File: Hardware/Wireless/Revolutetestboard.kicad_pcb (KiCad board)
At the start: 4 copper layers, 54 x 85.6 mm, 104 parts, among them J1 -, J2 +, J3 USB_C_Receptacle_USB2.0, J4 Conn_01x02_Pin, J5 USB_C_Receptacle_USB2.0, Q1 NMOS, Q2 NMOS-CSD17381F4, Q3 NMOS-CSD17381F4, Q4 PMOS-CSD25483F4, Q5 PMOS-CSD25483F4, SW1 SW_DIP_x05, U10 Button, U11 LSM6DSO, U12 STM32F103C8Tx, U13 AP2112K-3.3, U14 Conn_01x14_Socket, U2 nrf52833_qfn40, U3 AS5600, U4 MIC5504, U5 BQ24075RGT, U6 Button, U7 Conn_01x14_Socket, U8 Button, U9 Button, X1 32.768 kHz, X2 32MHZ, Y1 32.768KHZ, Y2 8Mhz

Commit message: new flex and new pcbs
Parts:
- removed ? (x2): , 
- added J6: Conn_01x04_Socket, Connector_PinSocket_2.54mm:PinSocket_1x04_P2.54mm_Vertical, F.Cu at (134.8, 140.0)
- added JP6: Jumper_3_Bridged12, Jumper:SolderJumper-3_P1.3mm_Bridged12_RoundedPad1.0x1.5mm, F.Cu at (146.7, 140.0)
- added R23: 2M, Library:Resistor_0402_1005M-nosilk, F.Cu at (153.9, 122.3)
- added SW2: SW_Push, Library:16mmCompButton, B.Cu at (148.5, 99.0)
- added TP1: TestPoint, TestPoint:TestPoint_Pad_D1.0mm, F.Cu at (151.7, 128.7)
- added TP10: TestPoint, TestPoint:TestPoint_Pad_D1.0mm, F.Cu at (146.0, 121.6)
- added TP11: TestPoint, TestPoint:TestPoint_Pad_D1.0mm, F.Cu at (155.2, 121.0)
- added TP12: TestPoint, TestPoint:TestPoint_Pad_D1.0mm, F.Cu at (149.5, 129.6)
- added TP13: TestPoint, TestPoint:TestPoint_Pad_D1.0mm, F.Cu at (141.9, 135.3)
- added TP2: TestPoint, TestPoint:TestPoint_Pad_D1.0mm, F.Cu at (147.9, 135.5)
- added TP3: TestPoint, TestPoint:TestPoint_Pad_D1.0mm, F.Cu at (133.6, 135.3)
- added TP4: TestPoint, TestPoint:TestPoint_Pad_D1.0mm, F.Cu at (114.7, 150.1)
- added TP5: TestPoint, TestPoint:TestPoint_Pad_D1.0mm, F.Cu at (128.1, 127.1)
- added TP6: TestPoint, TestPoint:TestPoint_Pad_D1.0mm, F.Cu at (130.9, 133.3)
- added TP7: TestPoint, TestPoint:TestPoint_Pad_D1.0mm, F.Cu at (130.4, 127.3)
- added TP8: TestPoint, TestPoint:TestPoint_Pad_D1.0mm, F.Cu at (151.4, 133.2)
- added TP9: TestPoint, TestPoint:TestPoint_Pad_D1.0mm, F.Cu at (143.1, 101.1)
- Q1: value NMOS -> PMOS-CSD25483F4
- moved C28 25.1 mm to (122.3, 145.8), turned to -90 degrees
- moved C29 23.9 mm to (121.3, 145.8), turned to -90 degrees
- moved U13 20.7 mm to (118.6, 146.3), turned to 180 degrees
- moved C32 15.8 mm to (117.5, 143.9)
- moved C33 15.3 mm to (119.4, 143.9), turned to 180 degrees
- moved JP4 8.67 mm to (136.8, 124.3), turned to 0 degrees
- moved J4 1.81 mm to (118.2, 141.0)
- moved C25 1.65 mm to (143.1, 131.6)
- moved TH1 1.62 mm to (143.5, 130.1)
- moved R7 1.44 mm to (144.9, 135.4)
- moved D2 1.41 mm to (149.9, 133.6), turned to 90 degrees
- moved R3 1.37 mm to (143.6, 133.8)
- moved R4 1.37 mm to (149.3, 131.1)
- moved R9 1.37 mm to (148.9, 133.6)
- moved U5 1.37 mm to (146.2, 132.3)
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- renumbered AE** to Antenna
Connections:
- Q1 pad 2: MOS_VDD -> VDD_nRF
- Q1 pad 3: VDD_nRF -> MOS_VDD
- SW1 pad 1: unconnected-(SW1-Pad1) -> VBUS
- SW1 pad 2: unconnected-(SW1-Pad2) -> swc
- SW1 pad 3: unconnected-(SW1-Pad3) -> swd
- SW1 pad 4: unconnected-(SW1-Pad4) -> D+
- SW1 pad 5: unconnected-(SW1-Pad5) -> D-
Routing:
- net swc: track 0.00 -> 67.4 mm, vias 0 -> 2
- net swd: track 0.00 -> 65.9 mm, vias 0 -> 2
- net Batteryin: track 0.00 -> 65.4 mm, vias 0 -> 3
- net MOS_VDD: track 0.00 -> 61.2 mm, vias 0 -> 10
- net VBUS: track 1.06 -> 61.9 mm, vias 0 -> 5
- net /USBDM2: track 0.00 -> 60.5 mm, vias 0 -> 2
- net /USBDP2: track 0.00 -> 60.2 mm, vias 0 -> 4
- net P0.28: track 0.00 -> 57.8 mm, vias 0 -> 2
- net P0.15: track 5.37 -> 59.0 mm, vias 0 -> 3
- net D-: track 0.00 -> 53.2 mm, vias 0 -> 2
- net P0.17: track 6.84 -> 59.8 mm, vias 0 -> 3
- net D+: track 0.00 -> 52.0 mm, vias 0 -> 2
- net /B14: track 0.00 -> 40.4 mm, vias 0 -> 3
- net /A5: track 0.00 -> 36.5 mm, vias 0 -> 3
- net P0.30: track 0.00 -> 33.6 mm
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- added copper zone on F.Cu, net 3.3V
- added copper zone on In2.Cu, net 3.3V
- added copper zone on In2.Cu, net 5V
- added copper zone on F.Cu, net MOS_VDD
- added copper zone on In2.Cu, net MOS_VDD
- added copper zone on F.Cu, net OUT
- added copper zone on F.Cu, net VBUS
- added copper zone on F.Cu, net VDD_nRF
- added copper zone on In2.Cu, net VDD_nRF
- added copper zone on F.Cu, net vBAT
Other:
- board text added: "3.3V"
- board text added: "3V"
- board text added: "3V supply"
- board text added: "5V"
- board text added: "FOR BOOTLOADER, Boot0=1 Boot1=0"
- board text added: "FOR OPERATION, Boot0=0 Boot1=0"
- board text added: "GND"
- board text added: "I2C"
- board text added: "LIR2032"
- board text added: "OUT"
- board text added: "Oct 20 2024"
- board text added: "RST"
- board text added: "Rev1"
- board text added: "Rx"
- board text added: "SCL"
- board text added: "SDA"
- board text added: "SWC"
- board text added: "SWD"
- board text added: "Test"
- board text added: "Tongtong.inc"
- board text added: "Tx"
- board text added: "VBAT"
- board text added: "VBUS"
- board text added: "VDD"
- board text added: "VDD MOS"
- board text added: "VDD NRF"
- board text added: "VDD_MOS"
- board text added: "current monitoring"

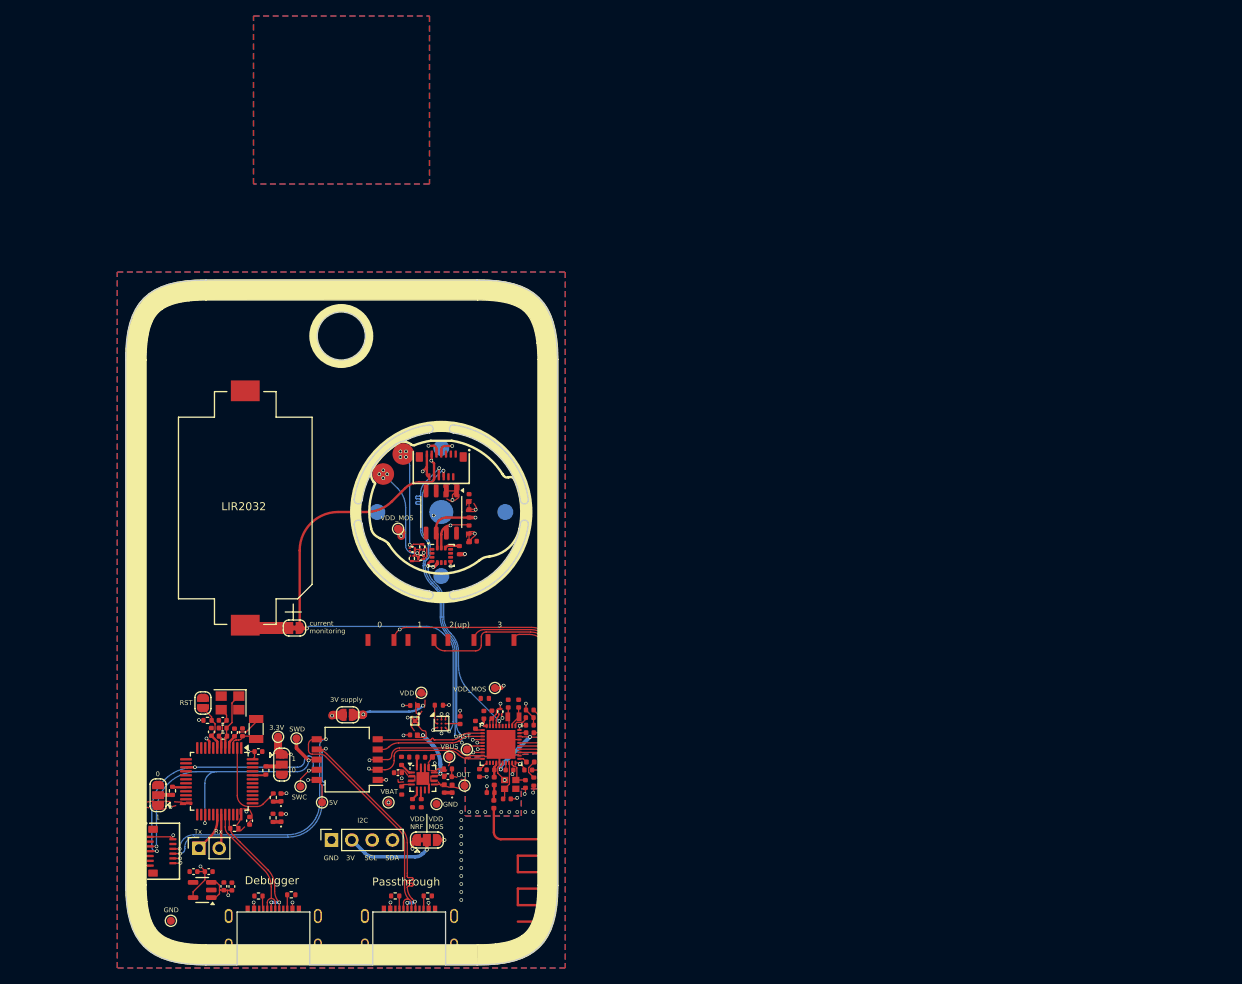
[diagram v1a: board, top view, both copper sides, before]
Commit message: unrouted test board
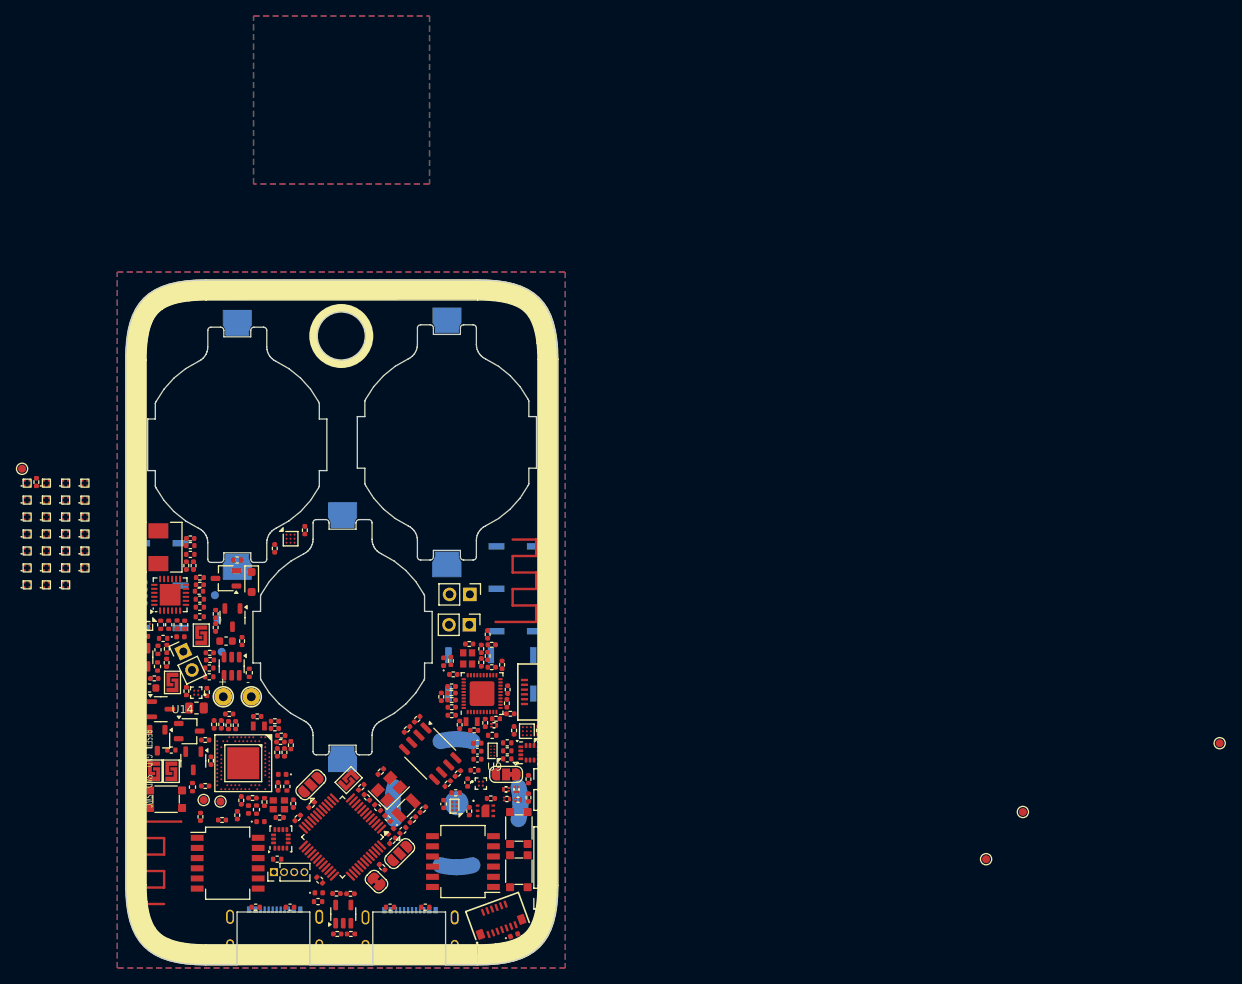
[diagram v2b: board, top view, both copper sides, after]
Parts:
- removed Antenna: 2.4GHz-meander-antenna, Library:2.4GHz-meander-antenna
- removed R7: 0Ω, Library:Resistor_0402_1005M-nosilk
- removed TP12, TP13, TP4: TestPoint, TestPoint:TestPoint_Pad_D1.0mm
- added AE1: Antenna, Library:2.4GHz-meander-antenna, F.Cu at (155.3, 112.7)
- added AE2: Antenna, Library:2.4GHz-meander-antenna, F.Cu at (116.0, 137.7)
- added BT2: Battery_Cell, Library:BatteryHolder_Keystone_1057_1x2032, B.Cu at (123.0, 90.6)
- added BT3: Battery_Cell, Library:BatteryHolder_Keystone_1057_1x2032, B.Cu at (136.2, 114.7)
- added C36: 22uF, Library:0402, F.Cu at (111.0, 108.7)
- added C37: 22uF, Library:0402, F.Cu at (111.0, 107.8)
- added C38: 100nF, Library:0402, F.Cu at (111.0, 110.4)
- added C39: 100nF, Library:0402, F.Cu at (111.0, 109.5)
- added C40: 10uF, Library:0402, F.Cu at (117.5, 105.7)
- added C41: 10uF, Library:0402, F.Cu at (118.3, 107.2)
- added C42: 10uF, Library:0402, F.Cu at (117.1, 102.3)
- added C43: 1uF, Library:0402, F.Cu at (128.9, 129.0)
- added C44: 47nF, Library:0402, F.Cu at (128.0, 129.0)
- added C45: 10uF, Library:0402, F.Cu at (118.3, 108.1)
- added C46: 100nF, Library:0402, F.Cu at (119.7, 130.1)
- added C47: 100nF, Library:0402, F.Cu at (128.1, 133.3)
- added C48: 100nF, Library:0402, F.Cu at (119.0, 133.2)
- added C49: 1pF, Library:0402, F.Cu at (124.9, 134.7)
- added C50: 1uF, Library:0402, F.Cu at (116.6, 121.4)
- added C51: 12pF, Library:0402, F.Cu at (130.0, 135.4)
- added C52: 12pF, Library:0402, F.Cu at (128.3, 137.2)
- added C53: 820pF, Library:0402, F.Cu at (123.5, 135.1)
- added C54: 100nF, Library:0402, F.Cu at (111.4, 114.5)
- added C55: 100pF, Library:0402, F.Cu at (126.4, 135.2)
- added C56: 1pF, Library:0402, F.Cu at (123.0, 136.9)
- added C57: 1.5pF, Library:0402, F.Cu at (118.4, 137.1)
- added C58: 2.2uF, Library:0402, F.Cu at (131.4, 101.3)
- added C59: 100nf, Library:0402, F.Cu at (119.2, 121.5)
- added C60: 1uF, Library:0402, F.Cu at (112.6, 119.8)
- added C61: 10nF, Library:0402, F.Cu at (120.3, 113.4)
- added C62: 100nF, Library:0402, F.Cu at (110.7, 119.8)
- added C63: 100nF, Library:0402, F.Cu at (123.6, 115.1)
- added C64: 56pF, Library:0402, F.Cu at (114.2, 116.1)
- added C65: 68pF, Library:0402, F.Cu at (119.6, 117.5)
- added C66: 47uF, Library:0402, F.Cu at (114.2, 117.8)
- added C67: 47uF, Library:0402, F.Cu at (119.6, 116.6)
- added C68: 12pF, Library:0402, F.Cu at (146.2, 136.2)
- added C69: 12pF, Library:0402, F.Cu at (144.9, 137.5)
- added C70: 100nF, Library:0402, F.Cu at (139.2, 134.7)
- added C71: 100nF, Library:0402, F.Cu at (135.5, 151.7)
- added C72: 10uF, Library:0402, F.Cu at (137.2, 151.7)
- added C73: 100nF, Library:0402, F.Cu at (130.6, 137.2)
- added C74: 100nF, Library:0402, F.Cu at (142.4, 140.1)
- added C75: 10uF, Library:0402, F.Cu at (135.4, 146.7)
- added C76: 100nF, Library:0402, F.Cu at (137.2, 146.7)
- added C77: 22pf, Library:0402, F.Cu at (140.9, 131.5)
- added C78: 22pf, Library:0402, F.Cu at (141.8, 137.3)
- added D10: argb_led, Library:Led-ARGB, F.Cu at (96.7, 103.9)
- added D11: argb_led, Library:Led-ARGB, F.Cu at (96.7, 106.0)
- added D12: argb_led, Library:Led-ARGB, F.Cu at (96.7, 108.1)
- added D13: argb_led, Library:Led-ARGB, F.Cu at (99.1, 95.4)
- added D14: argb_led, Library:Led-ARGB, F.Cu at (99.1, 97.5)
- added D15: argb_led, Library:Led-ARGB, F.Cu at (99.1, 99.6)
- added D16: argb_led, Library:Led-ARGB, F.Cu at (99.1, 101.8)
- added D17: argb_led, Library:Led-ARGB, F.Cu at (99.1, 103.9)
- added D18: argb_led, Library:Led-ARGB, F.Cu at (99.1, 106.0)
- added D19: argb_led, Library:Led-ARGB, F.Cu at (99.1, 108.1)
- added D20: argb_led, Library:Led-ARGB, F.Cu at (101.5, 95.4)
- added D21: argb_led, Library:Led-ARGB, F.Cu at (101.5, 97.5)
- added D22: argb_led, Library:Led-ARGB, F.Cu at (101.5, 99.6)
- added D23: argb_led, Library:Led-ARGB, F.Cu at (101.5, 101.8)
- added D24: argb_led, Library:Led-ARGB, F.Cu at (101.5, 103.9)
- added D25: argb_led, Library:Led-ARGB, F.Cu at (101.5, 106.0)
- added D26: argb_led, Library:Led-ARGB, F.Cu at (101.5, 108.1)
- added D27: argb_led, Library:Led-ARGB, F.Cu at (104.0, 95.4)
- added D28: argb_led, Library:Led-ARGB, F.Cu at (104.0, 97.5)
- added D29: argb_led, Library:Led-ARGB, F.Cu at (104.0, 99.6)
- added D30: argb_led, Library:Led-ARGB, F.Cu at (104.0, 101.8)
- added D31: argb_led, Library:Led-ARGB, F.Cu at (104.0, 103.9)
- added D32: argb_led, Library:Led-ARGB, F.Cu at (104.0, 106.0)
- added D33: BLUE, LED_SMD:LED_0402_1005Metric, F.Cu at (133.2, 146.6)
- added D34: White, LED_SMD:LED_0402_1005Metric, F.Cu at (142.2, 138.9)
- added D35: White, LED_SMD:LED_0402_1005Metric, F.Cu at (157.6, 151.9)
- added D5: 1N5819, Diode_SMD:D_SOD-323_HandSoldering, F.Cu at (124.8, 107.8)
- added D6: argb_led, Library:Led-ARGB, F.Cu at (96.7, 95.4)
- added D7: argb_led, Library:Led-ARGB, F.Cu at (96.7, 97.5)
- added D8: argb_led, Library:Led-ARGB, F.Cu at (96.7, 99.6)
- added D9: argb_led, Library:Led-ARGB, F.Cu at (96.7, 101.8)
- added F1: Polyfuse, Resistor_SMD:R_0805_2012Metric, F.Cu at (117.9, 123.5)
- added J7: USB_C_Receptacle_USB2.0, Library:USB-C_C168688, B.Cu at (127.7, 155.7)
- added J8: USB_C_Receptacle_USB2.0, Library:USB-C_C168688, B.Cu at (144.6, 155.8)
- added JP7: Jumper_3_Open, Jumper:SolderJumper-3_P1.3mm_Open_RoundedPad1.0x1.5mm, F.Cu at (132.2, 133.1)
- added JP8: Jumper_3_Open, Jumper:SolderJumper-3_P1.3mm_Open_RoundedPad1.0x1.5mm, F.Cu at (143.3, 141.7)
- added JP9: Jumper_2_Bridged, Jumper:SolderJumper-2_P1.3mm_Bridged_RoundedPad1.0x1.5mm, F.Cu at (140.4, 145.2)
- added L10: 12uH, Inductor_SMD:L_0603_1608Metric, F.Cu at (121.6, 115.1)
- added L5: 2.2uH, Inductor_SMD:L_Chilisin_BMRA00050520, F.Cu at (113.1, 103.4)
- added L6: 15nH, Library:0402, F.Cu at (129.7, 128.2)
- added L7: 10uH, Library:0402, F.Cu at (128.4, 127.7)
- added L8: 3.9nH, Inductor_SMD:L_0402_1005Metric, F.Cu at (124.4, 136.2)
- added L9: 12uH, Inductor_SMD:L_0603_1608Metric, F.Cu at (112.0, 121.0)
- added Q10: PMOS-BSS84, Package_TO_SOT_SMD:SOT-23-3, F.Cu at (117.5, 130.1)
- added Q7: PMOS-BSS84, Package_TO_SOT_SMD:SOT-23-3, F.Cu at (113.4, 123.7)
- added Q8: IRLML6344, Package_TO_SOT_SMD:TSOT-23, F.Cu at (121.6, 107.3)
- added Q9: PMOS-BSS84, Package_TO_SOT_SMD:SOT-23-3, F.Cu at (122.4, 112.2)
- added R24: 91K, Resistor_SMD:R_0402_1005Metric, F.Cu at (118.2, 108.9)
- added R25: 4.7K, Library:0402, F.Cu at (122.8, 125.6)
- added R26: 100r, Resistor_SMD:R_0402_1005Metric, F.Cu at (110.9, 111.4)
- added R27: 0.5r, Resistor_SMD:R_0402_1005Metric, F.Cu at (117.1, 104.3)
- added R28: 5.1K, Resistor_SMD:R_0402_1005Metric, F.Cu at (117.1, 103.2)
- added R29: 1K, Resistor_SMD:R_0402_1005Metric, F.Cu at (125.4, 136.2)
- added R30: 1K, Resistor_SMD:R_0402_1005Metric, F.Cu at (129.2, 133.3)
- added R31: 10k, Library:0402, F.Cu at (127.7, 103.6)
- added R32: 50r, Resistor_SMD:R_0402_1005Metric, F.Cu at (109.8, 113.5)
- added R33: 0r, Library:0402, F.Cu at (121.1, 137.5)
- added R34: 2M, Library:0402, F.Cu at (110.9, 123.0)
- added R35: 10K, Resistor_SMD:R_0402_1005Metric, F.Cu at (114.8, 128.8)
- added R36: 100K, Resistor_SMD:R_0402_1005Metric, F.Cu at (123.0, 105.0)
- added R37: 10K, Resistor_SMD:R_0402_1005Metric, F.Cu at (128.0, 142.4)
- added R38: 2M, Library:0402, F.Cu at (120.3, 111.7)
- added R39: 442K, Resistor_SMD:R_0402_1005Metric, F.Cu at (113.0, 118.3)
- added R40: 442K, Resistor_SMD:R_0402_1005Metric, F.Cu at (124.5, 119.1)
- added R41: 100K, Resistor_SMD:R_0402_1005Metric, F.Cu at (113.1, 116.2)
- added R42: 22K, Resistor_SMD:R_0402_1005Metric, F.Cu at (113.7, 114.8)
- added R43: 100K, Resistor_SMD:R_0402_1005Metric, F.Cu at (119.5, 118.5)
- added R44: 13K, Resistor_SMD:R_0402_1005Metric, F.Cu at (119.5, 119.6)
- added R45: 2M, Library:0402, F.Cu at (119.0, 127.5)
- added R46: 0r, Library:0402, F.Cu at (97.9, 95.3)
- added R47: 10k, Library:0402, F.Cu at (141.1, 143.4)
- added R48: 10k, Library:0402, F.Cu at (132.3, 135.6)
- added R49: 10k, Library:0402, F.Cu at (138.5, 133.4)
- added R50: 1.5K, Resistor_SMD:R_0402_1005Metric, F.Cu at (133.3, 145.0)
- added R51: 510Ω, Resistor_SMD:R_0402_1005Metric, F.Cu at (133.1, 147.7)
- added R52: 510Ω, Resistor_SMD:R_0402_1005Metric, F.Cu at (143.7, 138.8)
- added R53: 1M, Resistor_SMD:R_0402_1005Metric, F.Cu at (140.5, 136.0)
- added R54: 5.1K, Resistor_SMD:R_0402_1005Metric, F.Cu at (125.3, 148.4)
- added R55: 5.1K, Resistor_SMD:R_0402_1005Metric, F.Cu at (129.6, 148.4)
- added R56: 5.1K, Resistor_SMD:R_0402_1005Metric, F.Cu at (142.1, 148.4)
- added R57: 5.1K, Resistor_SMD:R_0402_1005Metric, F.Cu at (146.5, 148.4)
- added S2: Button 3*3*1.5, Library:button 3x3, F.Cu at (158.2, 138.5)
- added S3: Button 3*3*1.5, Library:button 3x3, F.Cu at (158.2, 143.9)
- added S4: Button 3*3*1.5, Library:button 3x3, F.Cu at (114.1, 134.9)
- added SW3: SW_DIP_x06, Button_Switch_SMD:SW_DIP_SPSTx06_Slide_Copal_CHS-06B_W7.62mm_P1.27mm, F.Cu at (121.8, 142.9)
- added SW4: SW_Push, Library:16mmCompButton, B.Cu at (150.4, 135.4)
- added SW5: SW_DPDT_x2, Library:MST-12C05 SLIDEBUTTON, B.Cu at (157.8, 108.6)
- added SW6: SW_DPDT_x2, Library:MST-12C05 SLIDEBUTTON, B.Cu at (113.5, 108.2)
- added U15: A3144e, Package_TO_SOT_SMD:TSOT-23, F.Cu at (117.0, 126.4)
- added U16: A3144e, Package_TO_SOT_SMD:TSOT-23, F.Cu at (113.0, 127.5)
- added U17: ~, Library:debug pins, F.Cu at (110.3, 131.3)
- added U18: pogopins, Library:pogopin, F.Cu at (123.0, 122.1)
- added U19: LSM6DS3, Package_LGA:LGA-14_3x2.5mm_P0.5mm_LayoutBorder3x4y, F.Cu at (128.4, 139.9)
- added U20: TPS54202DDC, Package_TO_SOT_SMD:SOT-23-6, F.Cu at (110.9, 117.2)
- added U21: TPS54202DDC, Package_TO_SOT_SMD:SOT-23-6, F.Cu at (122.3, 118.3)
- added U22: STM32F103CBTx, Package_QFP:LQFP-48_7x7mm_P0.5mm, F.Cu at (136.1, 139.6)
- added U23: AP2112K-3.3, Package_TO_SOT_SMD:SOT-23-5, F.Cu at (136.3, 149.3)
- added U24: Conn_01x14_Socket, Library:FPC, F.Cu at (155.6, 149.9)
- added X3: 32.768 kHz, Library:Crystal_SMD_2012-2Pin_2.0x1.2mm, F.Cu at (125.7, 125.7)
- added X4: 32MHZ, Library:Crystal_SMD_2016-4Pin_2.0x1.6mm, F.Cu at (128.2, 135.6)
- BT1: footprint Battery:BatteryHolder_Keystone_1060_1x2032 -> Library:BatteryHolder_Keystone_1057_1x2032; moved to B.Cu
- C1, C2, C22, C3, C9: footprint Library:Capacitor_0402_1005M-nosilk -> Library:0402
- C10: value 12pF -> 47nF; footprint Capacitor_SMD:C_0402_1005Metric -> Library:0402
- C11: value 47nF -> 100nF; footprint Library:Capacitor_0402_1005M-nosilk -> Library:0402
- C12: value 2.2uF -> 820pF; footprint Library:Capacitor_0402_1005M-nosilk -> Library:0402
- C13: value 100nF -> 1pF; footprint Library:Capacitor_0402_1005M-nosilk -> Library:0402
- C14: value 820pF -> 12pF; footprint Library:Capacitor_0402_1005M-nosilk -> Library:0402
- C15: value 1pF -> 12pF; footprint Library:Capacitor_0402_1005M-nosilk -> Library:0402
- C16: value 12pF -> 100pF; footprint Library:Capacitor_0402_1005M-nosilk -> Library:0402
- C17: value 12pF -> 1.2pF; footprint Library:Capacitor_0402_1005M-nosilk -> Library:0402
- C18: value 100pF -> 100nF; footprint Library:Capacitor_0402_1005M-nosilk -> Library:0402
- C19: value 1.2pF -> 2.2uF; footprint Library:Capacitor_0402_1005M-nosilk -> Library:0402
- C20: value 100nF -> 1uF; footprint Library:Capacitor_0402_1005M-nosilk -> Library:0402
- C21, C24: footprint Library:Capacitor_0402_1005M-nosilk -> Capacitor_SMD:C_0402_1005Metric
- C23: value 1uF -> 10uF; footprint Library:Capacitor_0402_1005M-nosilk -> Capacitor_SMD:C_0402_1005Metric
- C25: value 10uF -> 100nF
- C26: value 10uF -> 1uF
- C27: value 100nF -> 100nf
- C28: value 100nF -> 12pF; footprint Capacitor_SMD:C_0402_1005Metric -> Library:0402
- C29: value 10uF -> 12pF; footprint Capacitor_SMD:C_0402_1005Metric -> Library:0402
- C30, C31, C33: value 100nF -> 4.7uF; footprint Capacitor_SMD:C_0402_1005Metric -> Library:0402
- C32: value 10uF -> 100nF; footprint Capacitor_SMD:C_0402_1005Metric -> Library:0402
- C34: value 22pf -> 1uF; footprint Capacitor_SMD:C_0402_1005Metric -> Library:0402
- C35: value 22pf -> 100nF; footprint Capacitor_SMD:C_0402_1005Metric -> Library:0402
- C4: value 12pF -> 100nF; footprint Capacitor_SMD:C_0402_1005Metric -> Library:0402
- C5: value 100nF -> 4.7uF; footprint Library:Capacitor_0402_1005M-nosilk -> Library:0402
- C6: value 4.7uF -> 1uF; footprint Library:Capacitor_0402_1005M-nosilk -> Library:0402
- C7: value 1uF -> 4.7uF; footprint Library:Capacitor_0402_1005M-nosilk -> Library:0402
- C8: value 4.7uF -> 2.2uF; footprint Library:Capacitor_0402_1005M-nosilk -> Library:0402
- D3: value BLUE -> RED_LED
- D4: value White -> WHITE_LED
- J1: value - -> Conn_01x02_Pin; footprint Library:Pogo-pin-recepticle -> Connector_PinHeader_2.54mm:PinHeader_1x02_P2.54mm_Vertical
- J2: value + -> Conn_01x02_Pin; footprint Library:Pogo-pin-recepticle -> Connector_PinHeader_2.54mm:PinHeader_1x02_P2.54mm_Vertical
- J3, J5: value USB_C_Receptacle_USB2.0 -> Conn_01x02_Pin; footprint Library:USB-C_C168688 -> Connector_PinHeader_2.54mm:PinHeader_1x02_P2.54mm_Vertical
- J4: value Conn_01x02_Pin -> Conn_01x04_Socket; footprint Connector_PinSocket_2.54mm:PinSocket_1x02_P2.54mm_Vertical -> Connector_PinSocket_2.54mm:PinSocket_1x04_P2.54mm_Vertical
- J6: value Conn_01x04_Socket -> Conn_01x04_Pin; footprint Connector_PinSocket_2.54mm:PinSocket_1x04_P2.54mm_Vertical -> Connector_PinHeader_1.27mm:PinHeader_1x04_P1.27mm_Vertical
- JP1: value SolderJumper_2_Open -> Jumper_3_Bridged12; footprint Jumper:SolderJumper-2_P1.3mm_Open_RoundedPad1.0x1.5mm -> Jumper:SolderJumper-3_P1.3mm_Bridged12_RoundedPad1.0x1.5mm
- JP2, JP3: value Jumper_3_Open -> SolderJumper_2_Open; footprint Jumper:SolderJumper-3_P1.3mm_Open_RoundedPad1.0x1.5mm -> Library:SolderBridge
- JP4: value Jumper_2_Open -> SolderJumper_2_Open; footprint Jumper:SolderJumper-2_P1.3mm_Open_RoundedPad1.0x1.5mm -> Library:SolderBridge
- JP5: value Jumper_2_Bridged -> SolderJumper_2_Open; footprint Jumper:SolderJumper-2_P1.3mm_Bridged_RoundedPad1.0x1.5mm -> Library:SolderBridge
- JP6: value Jumper_3_Bridged12 -> SolderJumper_2_Open; footprint Jumper:SolderJumper-3_P1.3mm_Bridged12_RoundedPad1.0x1.5mm -> Library:SolderBridge
- L1, L2, L3, L4: footprint Inductor_SMD:L_0402_1005Metric -> Library:0402
- Q1: value PMOS-CSD25483F4 -> NMOS-CSD17381F4
- Q3: value NMOS-CSD17381F4 -> PMOS-CSD25483F4
- R1: value 10k -> 0r; footprint Library:Resistor_0402_1005M-nosilk -> Library:0402
- R10: value 0Ω -> 3k; footprint Library:Resistor_0402_1005M-nosilk -> Resistor_SMD:R_0402_1005Metric
- R11: value 10k -> 4.7K; footprint Library:Resistor_0402_1005M-nosilk -> Library:0402
- R12: value 5.1K -> 4.7K; footprint Resistor_SMD:R_0402_1005Metric -> Library:0402
- R13: value 5.1K -> 10k; footprint Resistor_SMD:R_0402_1005Metric -> Library:0402
- R14: value 10k -> 50r
- R15: value 10k -> 1K
- R16: value 10k -> 5.1K
- R17: value 1.5K -> 4.7K; footprint Resistor_SMD:R_0402_1005Metric -> Library:0402
- R18: value 510Ω -> 120K
- R19: value 510Ω -> 51K
- R2: value 1.5k -> 0r; footprint Library:Resistor_0402_1005M-nosilk -> Library:0402
- R20: value 1M -> 1K
- R21, R22: value 5.1K -> 68K
- R23: value 2M -> 120K; footprint Library:Resistor_0402_1005M-nosilk -> Resistor_SMD:R_0402_1005Metric
- R3: value 100K -> 10k; footprint Library:Resistor_0402_1005M-nosilk -> Library:0402
- R4: value 1.1k -> 1.5k; footprint Library:Resistor_0402_1005M-nosilk -> Library:0402
- R5: value 590 -> 1.5k; footprint Library:Resistor_0402_1005M-nosilk -> Library:0402
- R6: value 4.7K -> 2M; footprint Library:Resistor_0402_1005M-nosilk -> Library:0402
- R8: value 4.7K -> 10K; footprint Library:Resistor_0402_1005M-nosilk -> Resistor_SMD:R_0402_1005Metric
- R9: value 1.5k -> 10K; footprint Library:Resistor_0402_1005M-nosilk -> Resistor_SMD:R_0402_1005Metric
- SW1: value SW_DIP_x05 -> SW_DIP_x06; footprint Button_Switch_SMD:SW_DIP_SPSTx05_Slide_KingTek_DSHP05TS_W7.62mm_P1.27mm -> Button_Switch_SMD:SW_DIP_SPSTx06_Slide_Copal_CHS-06B_W7.62mm_P1.27mm
- SW2: value SW_Push -> SW_DPDT_x2; footprint Library:16mmCompButton -> Library:MST-12C05 SLIDEBUTTON
- TH1: footprint Library:Resistor_0402_1005M-nosilk -> Resistor_SMD:R_0402_1005Metric
- TP6, TP7, TP9: moved to B.Cu
- U1: value ~ -> BQ27427; footprint Package_BGA:Texas_DSBGA-9_1.62mmx1.58mm_Layout3x3_P0.5mm -> Library:Texas_DSBGA-9_1.62mmx1.58mm_Layout3x3_P0.5mm
- U10: value Button -> battery_charger; footprint Library:SMDButton -> Package_DFN_QFN:QFN-24-1EP_4x4mm_P0.5mm_EP2.7x2.6mm
- U11: value LSM6DSO -> nRF52840_aQFN73; footprint Package_LGA:LGA-14_3x2.5mm_P0.5mm_LayoutBorder3x4y -> Library:AQFN-73-1EP_7x7mm_P0.5mm_NRF52840-custom
- U12: value STM32F103C8Tx -> TS5A3159AYZPR; footprint Package_QFP:LQFP-48_7x7mm_P0.5mm -> Package_BGA:Texas_DSBGA-6_0.9x1.4mm_Layout2x3_P0.5mm
- U13: value AP2112K-3.3 -> BQ27427; footprint Package_TO_SOT_SMD:SOT-23-5 -> Package_BGA:Texas_DSBGA-9_1.62mmx1.58mm_Layout3x3_P0.5mm
- U14: value Conn_01x14_Socket -> TPS22910A; footprint Library:FPC -> Library:BGA4N50P2X2_88X88X50N
- U2: footprint Library:QFN-40-1EP_5x5mm_P0.4mm_EP3.6x3.6mm -> Library:nrf52833
- U3: value AS5600 -> Conn_01x14_Socket; footprint Library:SOIC-8-1EP_3.9x4.9mm_P1.27mm_EP2.514x3.2mm -> Library:FPC
- U4: value MIC5504 -> TPS709; footprint Library:TDFN-4 -> Library:DRV 6PIN
- U5: value BQ24075RGT -> AS5600; footprint Package_DFN_QFN:VQFN-16-1EP_3x3mm_P0.5mm_EP1.6x1.6mm -> Library:SOIC-8-1EP_3.9x4.9mm_P1.27mm_EP2.514x3.2mm
- U6: value Button -> BQ25180; footprint Library:SMDButton -> Package_BGA:Texas_DSBGA-8_0.705x1.468mm_Layout2x4_P0.4mm
- U7: value Conn_01x14_Socket -> LSM6DSO; footprint Library:FPC -> Package_LGA:LGA-14_3x2.5mm_P0.5mm_LayoutBorder3x4y
- U8: value Button -> TS5A3159AYZPR; footprint Library:SMDButton -> Package_BGA:Texas_DSBGA-6_0.9x1.4mm_Layout2x3_P0.5mm
- U9: value Button -> TPS22910A; footprint Library:SMDButton -> Library:BGA4N50P2X2_88X88X50N
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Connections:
- net BLUE_LED renamed /rev/BLUE_LED
- net GPOUT renamed /rev/GPOUT
- C1 pad 2: VDD_nRF -> /rev/VDD_nRF
- C10 pad 1: Net-(U12-PC15) -> Net-(U2-DEC4)
- C11 pad 1: Net-(U2-DEC4) -> /rev/VDD_nRF
- C12 pad 1: 1.8V -> GND
- C12 pad 2: GND -> Net-(U2-DEC5)
- C13 pad 1: VDD_nRF -> GND
- C13 pad 2: GND -> Net-(U2-ANT)
- C14 pad 2: Net-(U2-DEC5) -> Net-(U2-XC2)
- C15 pad 2: Net-(U2-ANT) -> Net-(U2-XC1)
- C16 pad 2: Net-(U2-XC2) -> Net-(U2-DEC3)
- C17 pad 2: Net-(U2-XC1) -> Net-(C17-Pad2)
- C18 pad 1: GND -> /rev/MOS_VDD
- C18 pad 2: Net-(U2-DEC3) -> GND
- C19 pad 1: GND -> /rev/VDD_nRF
- C19 pad 2: Net-(C19-Pad2) -> GND
- C20 pad 1: MOS_VDD -> /rev/MOS_VDD
- C21 pad 1: MOS_VDD -> /rev/VBUS
- C22 pad 1: OUT -> /rev/vSYSTEM
- C23 pad 1: VDD_nRF -> /rev/vSYSTEM
- C24 pad 1: VBUS -> /rev/vBAT
- C25 pad 1: GND -> /rev/vSYSTEM
- C25 pad 2: vBAT -> GND
- C26 pad 1: OUT -> /rev/COM
- C27 pad 1: GND -> /rev/VBUS
- C27 pad 2: Net-(JP1-A) -> GND
- C28 pad 1: GND -> Net-(U11-XL1/P0.00)
- C28 pad 2: 5V -> GND
- C29 pad 1: GND -> Net-(U11-XL2/P0.01)
- C29 pad 2: 5V -> GND
- C30 pad 2: 3.3V -> /pod/3V
- C31 pad 2: 3.3V -> /pod/3V
- C32 pad 2: 3.3V -> Net-(U11-DEC1)
- C33 pad 2: 3.3V -> Net-(U11-DECUSB)
- C34 pad 2: /OSCIN -> /pod/3V
- C35 pad 1: GND -> Net-(U10-BST)
- C35 pad 2: /OSCOUT -> Net-(C35-Pad2)
- C4 pad 1: GND -> Net-(U2-DEC1)
- C4 pad 2: Net-(U12-PC14) -> GND
- C5 pad 1: Net-(U2-DEC1) -> /rev/VBUS
- C6 pad 1: VBUS -> /rev/VDD_nRF
- C7 pad 1: VDD_nRF -> GND
- C7 pad 2: GND -> Net-(U2-DECUSB)
- C8 pad 1: GND -> Net-(U1-VDD)
- C8 pad 2: Net-(U2-DECUSB) -> GND
- D2 pad 1: Net-(D2-K) -> GND
- D2 pad 2: OUT -> Net-(D2-A)
- D3 pad 2: 3.3V -> Net-(D3-A)
- D4 pad 2: 3.3V -> Net-(D4-A)
- J2 pad 1: Net-(J2-Pin_1) -> /rev/-
- J4 pad 1: /A9 -> GND
- J4 pad 2: /A10 -> Net-(J4-Pin_2)
- J6 pad 1: GND -> 5V
- J6 pad 2: Net-(J6-Pin_2) -> /dbg/TX
- J6 pad 3: P0.15 -> /dbg/RX
- J6 pad 4: P0.17 -> GND
- JP1 pad 1: Net-(JP1-A) -> /rev/MOS_VDD
- JP1 pad 2: GND -> Net-(J4-Pin_2)
- JP2 pad 1: 3.3V -> Net-(JP2-A)
- JP2 pad 2: /BOOT1 -> Net-(JP2-B)
- JP3 pad 1: 3.3V -> Net-(JP3-A)
- JP3 pad 2: /BOOT0 -> Net-(JP2-A)
- JP4 pad 1: 3.3V -> /pod/3V
- JP4 pad 2: VDD_nRF -> Net-(JP4-B)
- JP5 pad 1: Net-(BT1-+) -> /pod/5V
- JP5 pad 2: Batteryin -> Net-(JP5-B)
- JP6 pad 1: VDD_nRF -> Net-(JP6-A)
- JP6 pad 2: Net-(J6-Pin_2) -> GND
- L3 pad 2: Net-(C19-Pad2) -> Net-(C17-Pad2)
- L4 pad 1: Net-(C19-Pad2) -> Net-(C17-Pad2)
- L4 pad 2: antenna -> Net-(AE1-A)
- Q1 pad 1: MOS_EN -> /rev/+
- Q1 pad 2: VDD_nRF -> GND
- Q1 pad 3: MOS_VDD -> /rev/-
- Q2 pad 1: Net-(J2-Pin_1) -> /rev/-
- Q2 pad 3: Net-(J1-Pin_1) -> /rev/+
- Q3 pad 1: Net-(J1-Pin_1) -> /rev/+
- Q3 pad 2: GND -> /rev/COM
- Q3 pad 3: Net-(J2-Pin_1) -> /rev/-
- Q4 pad 1: Net-(J2-Pin_1) -> /rev/-
- Q4 pad 2: VBUS -> /rev/COM
- Q4 pad 3: Net-(J1-Pin_1) -> /rev/+
- Q5 pad 1: Net-(J1-Pin_1) -> /rev/MOS_EN
- Q5 pad 2: VBUS -> /rev/VDD_nRF
- Q5 pad 3: Net-(J2-Pin_1) -> /rev/MOS_VDD
- R1 pad 1: GND -> /rev/+
- R1 pad 2: Net-(U1-BIN) -> GND
- R10 pad 1: GND -> /rev/INT
- R10 pad 2: Net-(U5-EN1) -> /rev/VDD_nRF
- R11 pad 1: MOS_VDD -> /rev/MOS_VDD
- R11 pad 2: Net-(U11-CS) -> /rev/P0.15
- R12 pad 1: GND -> /rev/P0.17
- R12 pad 2: Net-(J3-CC2) -> /rev/MOS_VDD
- R13 pad 1: GND -> /rev/MOS_VDD
- R13 pad 2: Net-(J3-CC1) -> Net-(U7-CS)
- R14 pad 1: /BOOT0 -> GND
- R14 pad 2: Net-(U12-BOOT0) -> /rev/COM
- R15 pad 1: /BOOT1 -> Net-(D2-A)
- R15 pad 2: Net-(U12-PB2) -> /pod/LED6
- R16 pad 1: 3.3V -> Net-(JP2-A)
- R16 pad 2: Net-(JP1-A) -> /pod/3V
- R17 pad 1: 3.3V -> /pod/SCL
- R17 pad 2: /USBDP -> /pod/3V
- R18 pad 1: Net-(D3-K) -> GND
- R18 pad 2: GND -> Net-(U10-VSET)
- R19 pad 1: Net-(D4-K) -> GND
- R19 pad 2: /PC13 -> Net-(U10-NTC)
- R2 pad 1: GND -> /rev/-
- R2 pad 2: Net-(D1-K) -> Net-(SW2A-B)
- R20 pad 1: /OSCIN -> /pod/P0.14
- R20 pad 2: /OSCOUT -> Net-(U10-BAT_STAT)
- R21 pad 2: Net-(J5-CC2) -> Net-(U10-TIME_SET)
- R22 pad 2: Net-(J5-CC1) -> Net-(U10-VIN_UVSET)
- R23 pad 1: MOS_EN -> GND
- R23 pad 2: GND -> Net-(U10-VIN_OVSET)
- R3 pad 1: CE -> GND
- R3 pad 2: GND -> Net-(U1-BIN)
- R4 pad 1: Net-(U5-ILIM) -> /rev/FLEX_LED
- R4 pad 2: GND -> Net-(U2-P0.29/AIN5)
- R5 pad 1: Net-(U5-ISET) -> GND
- R5 pad 2: GND -> Net-(D1-K)
- R6 pad 1: MOS_VDD -> /rev/MOS_EN
- R6 pad 2: P0.15 -> GND
- R8 pad 1: MOS_VDD -> /rev/P0.17
- R8 pad 2: P0.17 -> /rev/VDD_nRF
- R9 pad 1: Net-(U5-~{CHG}) -> /rev/P0.15
- R9 pad 2: Net-(D2-K) -> /rev/VDD_nRF
- SW1 pad 1: VBUS -> /rev/VBUS
- SW1 pad 10: 5V -> /dbg/swd
- SW1 pad 2: swc -> /rev/swc
- SW1 pad 3: swd -> /rev/swd
- SW1 pad 4: D+ -> /rev/D+
- SW1 pad 5: D- -> /rev/D-
- SW1 pad 6: /USBDM2 -> /rev/FLEX_LED
- SW1 pad 7: /USBDP2 -> led
- SW1 pad 8: /B14 -> /dbg/USBDM2
- SW1 pad 9: /A5 -> /dbg/USBDP2
- SW2 pad 1: P0.28 -> /pod/COM
- SW2 pad 2: GND -> Net-(SW2A-B)
- TH1 pad 1: Net-(U5-TS) -> /rev/MR
- TP1 pad 1: RESET -> GND
- TP10 pad 1: VDD_nRF -> /pod/MOS_VDD
- TP11 pad 1: MOS_VDD -> Net-(D6-DI)
- TP2 pad 1: GND -> /rev/RESET
- TP3 pad 1: 5V -> Net-(U1-VDD)
- TP5 pad 1: 3.3V -> GND
- TP6 pad 1: /A5 -> /pod/VBUS
- TP7 pad 1: /B14 -> /pod/5V
- TP8 pad 1: OUT -> /pod/3V
- TP9 pad 1: MOS_VDD -> /pod/BAT_P
- U1 pad A2: P0.17 -> /rev/P0.17
- U1 pad A3: P0.15 -> /rev/P0.15
- U1 pad B3: 1.8V -> Net-(U1-VDD)
- U1 pad C2: vBAT -> /rev/vBAT
- U1 pad C3: Batteryin -> /rev/Batteryin
- U10 pad 2: GND -> unconnected-(U10-DP-Pad2)
- U10 pad 3: P0.28 -> Net-(U10-VSET)
- U2 pad 10: VBUS -> /rev/VBUS
- U2 pad 12: D- -> unconnected-(U2-D--Pad12)
- U2 pad 13: D+ -> unconnected-(U2-D+-Pad13)
- U2 pad 14: P0.15 -> /rev/P0.15
- U2 pad 15: P0.17 -> /rev/P0.17
- U2 pad 16: RESET -> /rev/RESET
- U2 pad 17: P0.20 -> /rev/INT
- U2 pad 18: VDD_nRF -> /rev/VDD_nRF
- U2 pad 19: swd -> /rev/swd
- U2 pad 20: swc -> /rev/swc
- U2 pad 22: unconnected-(U2-P0.09/NFC1-Pad22) -> /rev/P0.09
- U2 pad 23: unconnected-(U2-P0.10/NFC2-Pad23) -> /rev/P0.10
- U2 pad 30: VDD_nRF -> /rev/VDD_nRF
- U2 pad 32: unconnected-(U2-P0.02/AINO-Pad32) -> /rev/ON_TPS22910A
- U2 pad 33: P0.28 -> /rev/IN_TS5A3159AYZPR
- U2 pad 34: P0.29 -> Net-(U2-P0.29/AIN5)
- U2 pad 35: P0.30 -> /rev/LP
- U2 pad 36: P0.31 -> /rev/P0.31
- U2 pad 40: VDD_nRF -> /rev/VDD_nRF
- U2 pad 5: unconnected-(U2-P0.05/AIN3-Pad5) -> /rev/TX_TS5A3159AYZPR
- U2 pad 6: int1 -> /rev/int1
- U2 pad 7: MOS_EN -> /rev/MOS_EN
- U2 pad 8: VDD_nRF -> /rev/VDD_nRF
- U2 pad 9: VDD_nRF -> /rev/VDD_nRF
- U3 pad 1: MOS_VDD -> /rev/FLEX_LED
- U3 pad 2: MOS_VDD -> GND
- U3 pad 3: unconnected-(U3-OUT-Pad3) -> /rev/antenna
- U3 pad 6: P0.17 -> /rev/D+
- U3 pad 7: P0.15 -> /rev/swc
- U3 pad 8: unconnected-(U3-DIR-Pad8) -> /rev/D-
- U4 pad 1: VDD_nRF -> /rev/VDD_nRF
- U4 pad 2: GND -> unconnected-(U4-NC-Pad2)
- U4 pad 3: OUT -> GND
- U4 pad 4: OUT -> unconnected-(U4-EN-Pad4)
- U4 pad 5: GND -> unconnected-(U4-NC-Pad5)
- U5 pad 1: Net-(U5-TS) -> /rev/MOS_VDD
- U5 pad 2: vBAT -> /rev/MOS_VDD
- U5 pad 3: vBAT -> unconnected-(U5-OUT-Pad3)
- U5 pad 4: CE -> GND
- U5 pad 5: Net-(U5-EN2) -> GND
- U5 pad 6: Net-(U5-EN1) -> /rev/P0.17
- U5 pad 7: unconnected-(U5-~{PGOOD}-Pad7) -> /rev/P0.15
- U5 pad 8: GND -> unconnected-(U5-DIR-Pad8)
- U7 pad 1: GND -> unconnected-(U7-SDO/SA0-Pad1)
- U7 pad 10: Batteryin -> unconnected-(U7-NC-Pad10)
- U7 pad 11: Batteryin -> unconnected-(U7-NC-Pad11)
- U7 pad 12: VBUS -> Net-(U7-CS)
- U7 pad 13: VBUS -> /rev/P0.15
- U7 pad 14: unconnected-(U7-Pin_14-Pad14) -> /rev/P0.17
- U7 pad 2: GND -> unconnected-(U7-SDX-Pad2)
- U7 pad 4: GND -> /rev/int1
- U7 pad 5: GND -> /rev/MOS_VDD
- U7 pad 6: D+ -> GND
- U7 pad 7: swc -> GND
- U7 pad 8: D- -> /rev/MOS_VDD
- U7 pad 9: swd -> unconnected-(U7-INT2-Pad9)
- Y1 pad 1: Net-(U12-PC14) -> Net-(U22-PC14)
- Y1 pad 2: Net-(U12-PC15) -> Net-(U22-PC15)
- Y2 pad 1: /OSCOUT -> /dbg/OSCOUT
- Y2 pad 3: /OSCIN -> /dbg/OSCIN
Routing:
- net swc: track 67.4 -> 0.00 mm, vias 2 -> 0
- net swd: track 65.9 -> 0.00 mm, vias 2 -> 0
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- removed copper zone on F.Cu, net 3.3V
- removed copper zone on In2.Cu, net 3.3V
- removed copper zone on In2.Cu, net 5V
- removed copper zone on In2.Cu, net GND
- removed copper zone on F.Cu, net MOS_VDD
- removed copper zone on In2.Cu, net MOS_VDD
- removed copper zone on F.Cu, net OUT
- removed copper zone on F.Cu, net VBUS
- removed copper zone on F.Cu, net VDD_nRF
- removed copper zone on In2.Cu, net VDD_nRF
- removed copper zone on F.Cu, net vBAT
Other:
- outline, holes or cut-outs redrawn
- board text removed: "0"
- board text removed: "1"
- board text removed: "2(up)"
- board text removed: "3"
- board text removed: "3.3V"
- board text removed: "3V"
- board text removed: "3V supply"
- board text removed: "5V"
- board text removed: "GND"
- board text removed: "I2C"
- board text removed: "LIR2032"
- board text removed: "OUT"
- board text removed: "RST"
- board text removed: "Rx"
- board text removed: "SCL"
- board text removed: "SDA"
- board text removed: "SWC"
- board text removed: "SWD"
- board text removed: "System"
- board text removed: "Tx"
- board text removed: "VBAT"
- board text removed: "VBUS"
- board text removed: "VDD"
- board text removed: "VDD MOS"
- board text removed: "VDD NRF"
- board text removed: "VDD_MOS"
- board text removed: "current monitoring"

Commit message: added copper zone keep out for antenna
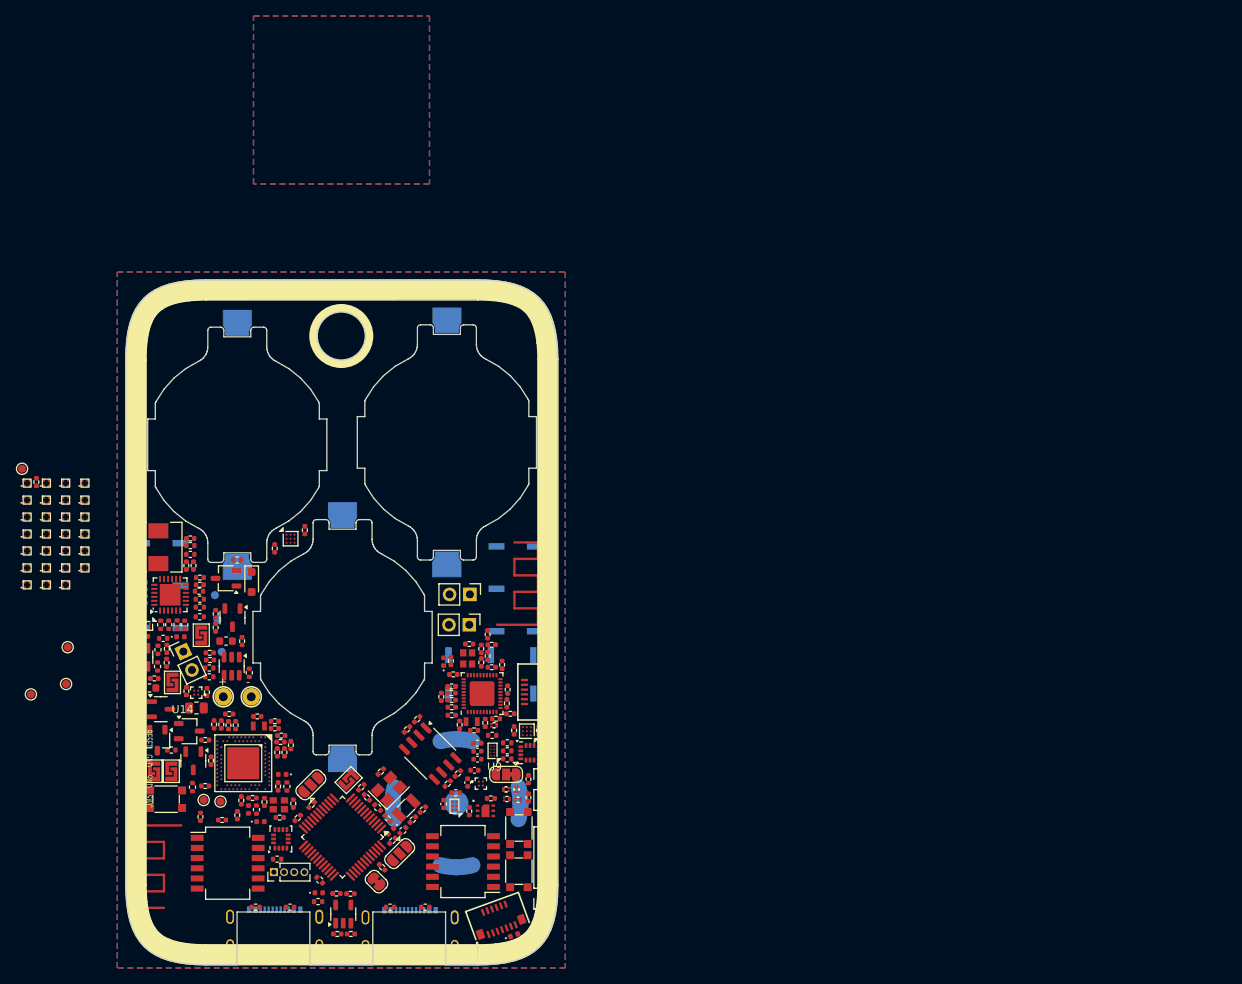
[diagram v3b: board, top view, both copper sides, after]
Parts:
- moved TP2 144.4 mm to (101.6, 120.5)
- moved TP1 121.2 mm to (97.2, 121.8)
- moved TP3 121.2 mm to (101.8, 115.9)
- moved AE2 0.48 mm to (116.0, 138.2)
- moved AE1 0.42 mm to (155.5, 113.1)
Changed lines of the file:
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@@
 	(footprint "TestPoint:TestPoint_Pad_D1.0mm"
 		(layer "F.Cu")
-		(at 221.2 136.5)
+		(at 101.8 115.9)
 		(descr "SMD pad as test Point, diameter 1.0mm")
 		(tags "test point SMD pad")
@@
 	(footprint "Library:2.4GHz-meander-antenna"
 		(layer "F.Cu")
-		(at 155.302787 112.742342 90)
+		(at 155.52 113.1 90)
 		(property "Reference" "AE1"
 			(at 0 -1.5 90)
@@
 	(footprint "Library:2.4GHz-meander-antenna"
 		(layer "F.Cu")
-		(at 115.98 137.7 -90)
+		(at 115.956075 138.178286 -90)
 		(property "Reference" "AE2"
 			(at 0 -1.5 -90)
@@
 	(footprint "TestPoint:TestPoint_Pad_D1.0mm"
 		(layer "F.Cu")
-		(at 245.8 127.9)
+		(at 101.6 120.5)
 		(descr "SMD pad as test Point, diameter 1.0mm")
 		(tags "test point SMD pad")
@@
 	(footprint "TestPoint:TestPoint_Pad_D1.0mm"
 		(layer "F.Cu")
-		(at 216.6 142.4)
+		(at 97.2 121.8)
 		(descr "SMD pad as test Point, diameter 1.0mm")
 		(tags "test point SMD pad")
@@
 		)
 	)
+	(zone
+		(net 0)
+		(net_name "")
+		(layers "F.Cu" "In1.Cu" "In2.Cu" "B.Cu")
+		(hatch edge 0.5)
+		(connect_pads
+			(clearance 0)
+		)
+		(min_thickness 0.25)
+		(filled_areas_thickness no)
+		(keepout
+			(tracks allowed)
+			(vias allowed)
+			(pads allowed)
+			(copperpour not_allowed)
+			(footprints allowed)
+		)
+		(fill
+			(thermal_gap 0.5)
+			(thermal_bridge_width 0.5)
+		)
+		(polygon
+			(pts
+				(xy 106.054567 136.864874) (xy 117.054567 136.864874) (xy 117.054567 155.864874) (xy 106.054567 155.864874)
+			)
+		)
+	)
+	(zone
+		(net 0)
+		(net_name "")
+		(layers "F.Cu" "In1.Cu" "In2.Cu" "B.Cu")
+		(hatch edge 0.5)
+		(connect_pads
+			(clearance 0)
+		)
+		(min_thickness 0.25)
+		(filled_areas_thickness no)
+		(keepout
+			(tracks allowed)
+			(vias allowed)
+			(pads allowed)
+			(copperpour not_allowed)
+			(footprints allowed)
+		)
+		(fill
+			(thermal_gap 0.5)
+			(thermal_bridge_width 0.5)
+		)
+		(polygon
+			(pts
+				(xy 155 102) (xy 159 99) (xy 165.915952 99) (xy 165.915952 116.055137) (xy 154.915952 116.055137)
+			)
+		)
+	)
